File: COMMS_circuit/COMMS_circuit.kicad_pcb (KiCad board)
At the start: 4 copper layers, 66.4 x 116 mm, 255 parts, among them J1 SMA, J2 SMA, J3 USB_C_Receptacle_USB2.0_14P, J4 Conn_01x02_Pin, J5 Conn_01x12_Pin, J7 USB_C_Receptacle_USB2.0, Q1 IRLML0060TRPBF, U1 max19713etn+, U10 FT2232HL, U11 93LC56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

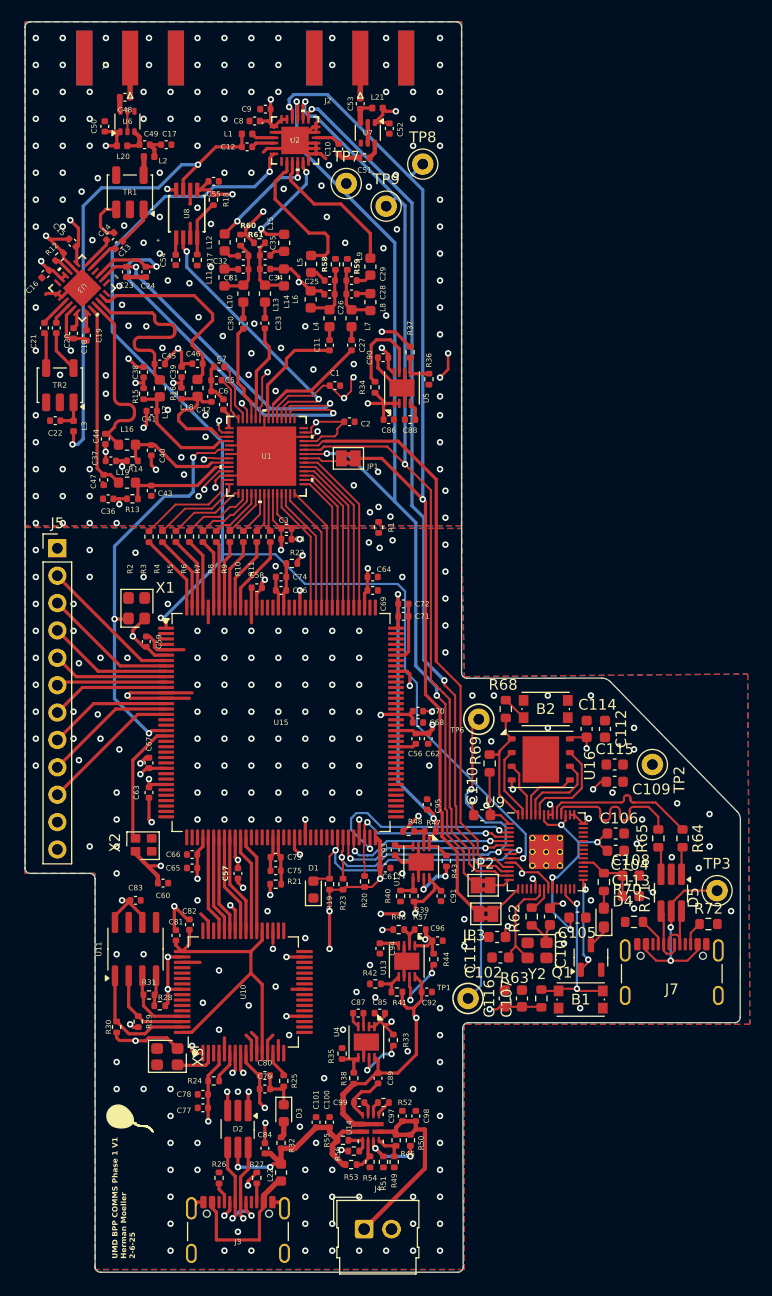
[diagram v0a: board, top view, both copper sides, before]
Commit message: switching the VBUS to RP2040 USB cause its more sensical
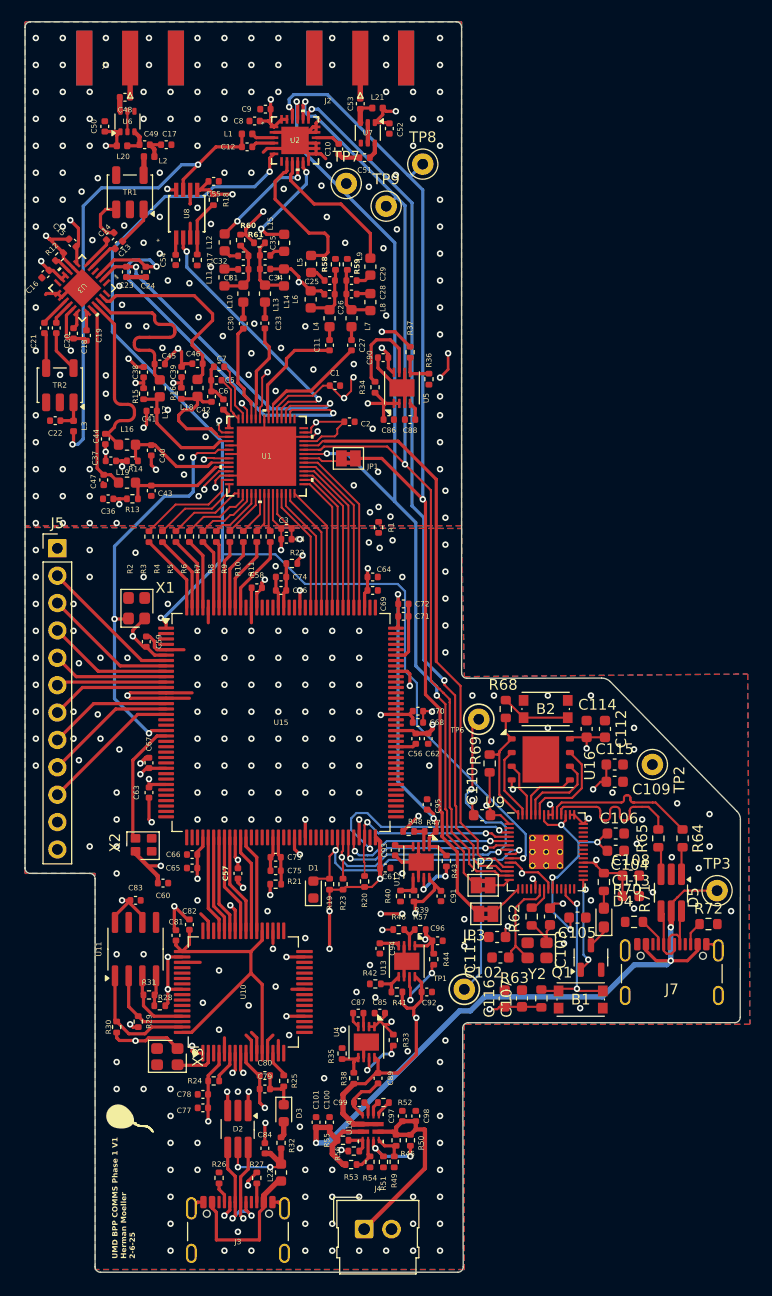
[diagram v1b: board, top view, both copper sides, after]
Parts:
- moved TP1 0.92 mm to (117.2, 118.2)
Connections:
- C84 pad 1: VBUS -> Net-(D2-VP)
- D2 pad 5: VBUS -> Net-(D2-VP)
- D5 pad 5: Net-(D5-VP) -> VBUS
- J7 pad A4: Net-(D5-VP) -> VBUS
- J7 pad A9: Net-(D5-VP) -> VBUS
- J7 pad B4: Net-(D5-VP) -> VBUS
- J7 pad B9: Net-(D5-VP) -> VBUS
- L22 pad 1: VBUS -> Net-(D2-VP)
- R32 pad 1: VBUS -> Net-(D2-VP)
- TP3 pad 1: Net-(D5-VP) -> VBUS
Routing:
- net VBUS: track 22.2 -> 66.9 mm, vias 2 -> 3
- net Net-(D5-VP): track 16.8 -> 0.00 mm, vias 2 -> 0
- net Net-(D2-VP): track 0.00 -> 9.31 mm, vias 0 -> 2
- net Net-(B2-Pad2): track 2.32 -> 6.42 mm
- net +3V3: track 175.1 -> 178.9 mm, vias 47 -> 48
- net DGND: track 99.8 -> 102.2 mm
- net /ICE_CDONE: track 39.6 -> 38.9 mm
- net AGND: vias 147 -> 148
